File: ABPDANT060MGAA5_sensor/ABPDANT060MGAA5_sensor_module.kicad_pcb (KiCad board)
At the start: 4 copper layers, 29 x 29.5 mm, 9 parts, among them J1 Conn_02x04_Odd_Even, J2 Conn_02x07_Odd_Even, U1 ABPDANT060MGAA5, U2 LM358

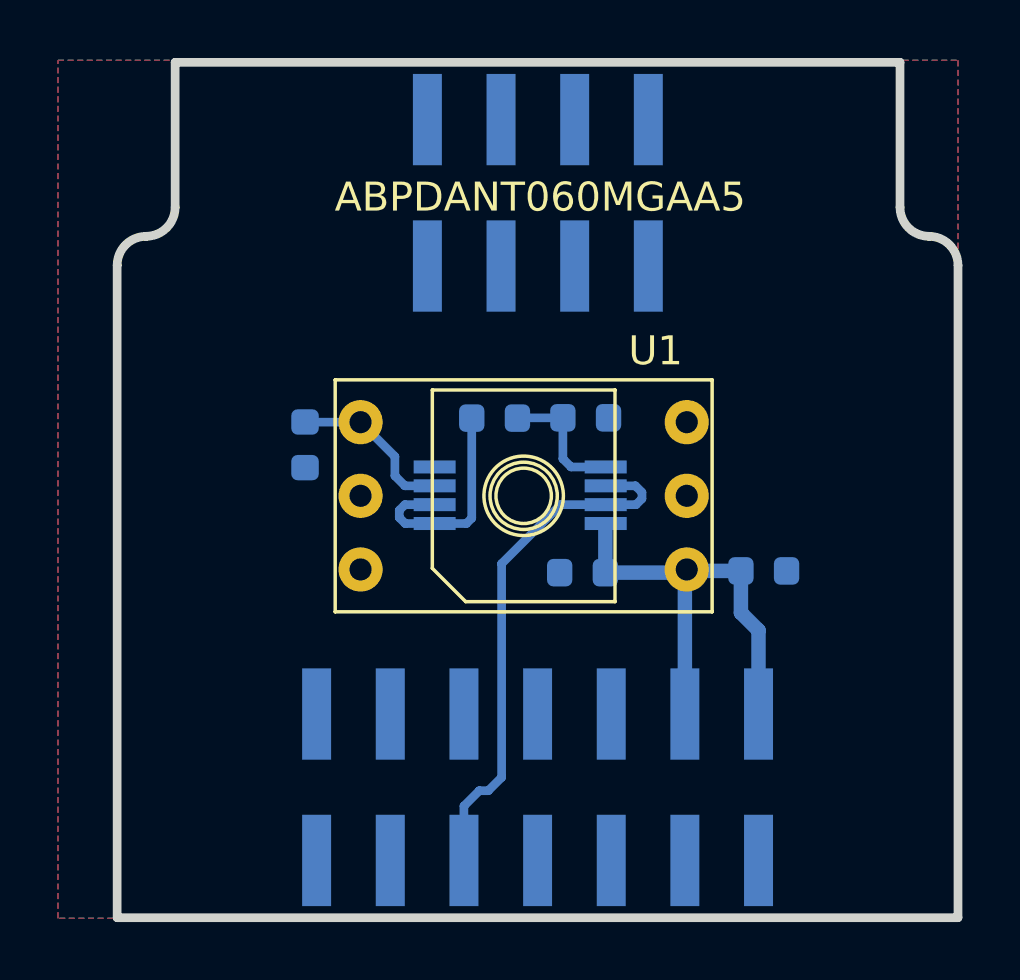
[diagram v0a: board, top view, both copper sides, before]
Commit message: Modified J2 position
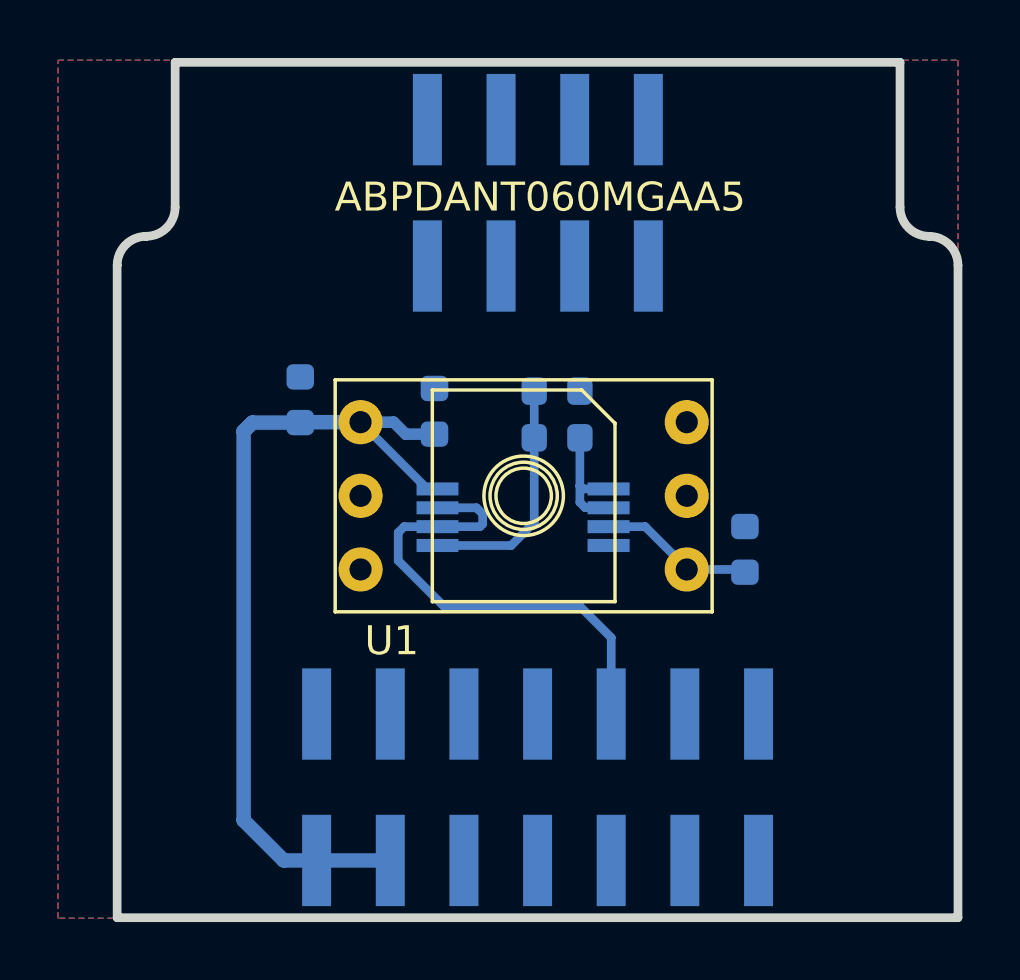
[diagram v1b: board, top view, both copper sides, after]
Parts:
- moved C1 17.0 mm to (104.8, 41.7), turned to 90 degrees
- moved C2 15.6 mm to (120.1, 46.9), turned to 90 degrees
- moved C3 7.55 mm to (109.4, 42.1), turned to 90 degrees
- moved R1 2.26 mm to (113.6, 43.0), turned to 0 degrees
- moved R2 1.35 mm to (113.6, 41.4)
- moved U2 0.76 mm to (112.4, 45.8), turned to 180 degrees
- turned J2 to 270 degrees
- turned U1 to 270 degrees
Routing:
- net +5V: track 21.2 -> 29.8 mm
- net Net-(R1-Pad1): track 4.58 -> 8.19 mm
- net Net-(R1-Pad2): track 7.66 -> 4.33 mm
- net /Analog: track 18.3 -> 17.1 mm
- net /SPI_CS: track 1.20 -> 0.00 mm

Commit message: Modified sensor modules and created module for 403-SFM3020 sensor
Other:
- rule pad_to_mask_clearance: 0.2 -> 0
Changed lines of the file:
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@@
-(kicad_pcb (version 20171130) (host pcbnew 5.1.10-88a1d61d58~90~ubuntu20.04.1)
+(kicad_pcb (version 20171130) (host pcbnew 5.1.12-84ad8e8a86~92~ubuntu20.04.1)
   (general
     (thickness 1.6)
@@
   )
   (setup
-    (last_trace_width 0.3)
+    (last_trace_width 0.2)
     (user_trace_width 0.2)
     (user_trace_width 0.3)
@@
     (pad_size 0.6 1.65)
     (pad_drill 0)
-    (pad_to_mask_clearance 0.2)
-    (solder_mask_min_width 0.2)
+    (pad_to_mask_clearance 0)
     (aux_axis_origin 0 0)
     (visible_elements FFFFFF7F)
     (pcbplotparams
-      (layerselection 0x010fc_ffffffff)
+      (layerselection 0x010fc_fffffff9)
       (usegerberextensions false)
       (usegerberattributes false)
@@
       (psa4output false)
       (plotreference true)
-      (plotvalue true)
+      (plotvalue false)
       (plotinvisibletext false)
       (padsonsilk false)
@@
     (pad 6 thru_hole circle (at -2.54 5.625 270) (size 1.524 1.524) (drill 0.762) (layers *.Cu *.Mask)
       (net 3 +5V))
+    (model ${KIPRJMOD}/../kicad-modules/shapes3d/abpdant005pgaa5.stp
+      (offset (xyz -40 -27.55 5))
+      (scale (xyz 1 1 1))
+      (rotate (xyz 0 0 -90))
+    )
   )
   (module Capacitor_SMD:C_0603_1608Metric (layer B.Cu)
